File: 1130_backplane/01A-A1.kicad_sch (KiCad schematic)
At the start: 86 parts

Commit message: Finish page KU201-KU211
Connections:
- net +CPU_STOP_LATCH: now reaches J84.b8 (Pin_b8)
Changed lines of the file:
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@@
+    (effects (font (size 1.27 1.27)) (justify left bottom))
+  )
+  (label "+CPU_STOP_LATCH" (at 807.72 236.22 0)
     (effects (font (size 1.27 1.27)) (justify left bottom))
   )

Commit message: Finish page KU301-KU311, minor column label fix.
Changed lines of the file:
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@@
     (effects (font (size 1.27 1.27)) (justify left bottom))
   )
-  (text "H" (at 482.6 90.17 0)
+  (text "H" (at 481.33 90.17 0)
     (effects (font (size 5 5) (thickness 1) bold) (justify left bottom))
   )
@@
     (effects (font (size 5 5) (thickness 1) bold) (justify left bottom))
   )
-  (text "H" (at 482.6 337.82 0)
+  (text "H" (at 481.33 337.82 0)
     (effects (font (size 5 5) (thickness 1) bold) (justify left bottom))
   )

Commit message: Finish page KW101. Add 48V bus for 01A-C1
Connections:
- net +CPU_RUN: now reaches J84.b6 (Pin_b6)
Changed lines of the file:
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@@
+    (effects (font (size 1.27 1.27)) (justify left bottom))
+  )
+  (label "+CPU_RUN" (at 807.72 231.14 0)
     (effects (font (size 1.27 1.27)) (justify left bottom))
   )

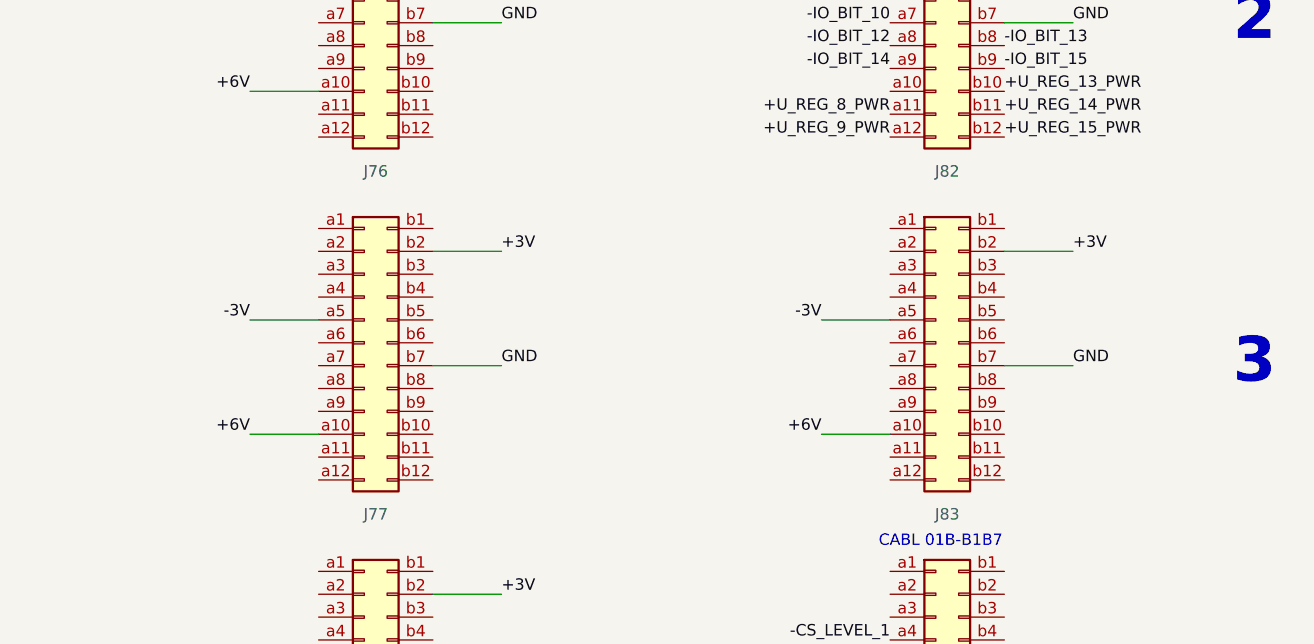
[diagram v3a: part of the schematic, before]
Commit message: Finish page RB301-RB321
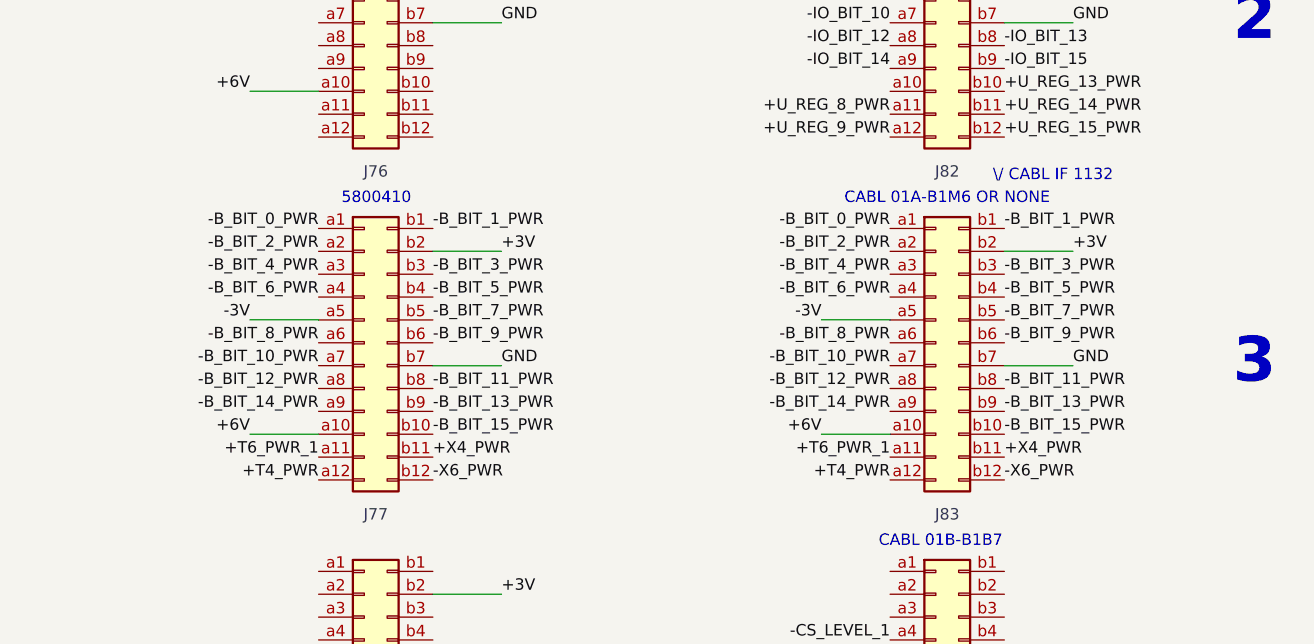
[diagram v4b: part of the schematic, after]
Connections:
- net -B_BIT_0_PWR: now reaches J76.a1 (Pin_a1)
- net -B_BIT_0_PWR: now also J82.a1 (Pin_a1)
- net +T6_PWR_1: now reaches J76.a11 (Pin_a11)
- net +T6_PWR_1: now also J82.a11 (Pin_a11)
- net +T4_PWR: now reaches J76.a12 (Pin_a12)
- net +T4_PWR: now also J82.a12 (Pin_a12)
- net -B_BIT_2_PWR: now reaches J76.a2 (Pin_a2)
- net -B_BIT_2_PWR: now also J82.a2 (Pin_a2)
- net -B_BIT_4_PWR: now reaches J76.a3 (Pin_a3)
- net -B_BIT_4_PWR: now also J82.a3 (Pin_a3)
- net -B_BIT_6_PWR: now reaches J76.a4 (Pin_a4)
- net -B_BIT_6_PWR: now also J82.a4 (Pin_a4)
- net -B_BIT_8_PWR: now reaches J76.a6 (Pin_a6)
- net -B_BIT_8_PWR: now also J82.a6 (Pin_a6)
- net -B_BIT_10_PWR: now reaches J76.a7 (Pin_a7)
- net -B_BIT_10_PWR: now also J82.a7 (Pin_a7)
- net -B_BIT_12_PWR: now reaches J76.a8 (Pin_a8)
- net -B_BIT_12_PWR: now also J82.a8 (Pin_a8)
- net -B_BIT_14_PWR: now reaches J76.a9 (Pin_a9)
- net -B_BIT_14_PWR: now also J82.a9 (Pin_a9)
- net -B_BIT_1_PWR: now reaches J76.b1 (Pin_b1)
- net -B_BIT_1_PWR: now also J82.b1 (Pin_b1)
- net -B_BIT_15_PWR: now reaches J76.b10 (Pin_b10)
- net -B_BIT_15_PWR: now also J82.b10 (Pin_b10)
- net +X4_PWR: now reaches J76.b11 (Pin_b11)
- net +X4_PWR: now also J82.b11 (Pin_b11)
- net -X6_PWR: now reaches J76.b12 (Pin_b12)
- net -X6_PWR: now also J82.b12 (Pin_b12)
- net -B_BIT_3_PWR: now reaches J76.b3 (Pin_b3)
- net -B_BIT_3_PWR: now also J82.b3 (Pin_b3)
- net -B_BIT_5_PWR: now reaches J76.b4 (Pin_b4)
- net -B_BIT_5_PWR: now also J82.b4 (Pin_b4)
- net -B_BIT_7_PWR: now reaches J76.b5 (Pin_b5)
- net -B_BIT_7_PWR: now also J82.b5 (Pin_b5)
- net -B_BIT_9_PWR: now reaches J76.b6 (Pin_b6)
- net -B_BIT_9_PWR: now also J82.b6 (Pin_b6)
- net -B_BIT_11_PWR: now reaches J76.b8 (Pin_b8)
- net -B_BIT_11_PWR: now also J82.b8 (Pin_b8)
- net -B_BIT_13_PWR: now reaches J76.b9 (Pin_b9)
- net -B_BIT_13_PWR: now also J82.b9 (Pin_b9)
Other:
- note added: "5800410"
- note added: "CABL 01A-B1M6 OR NONE"
- note added: "\/ CABL IF 1132"
